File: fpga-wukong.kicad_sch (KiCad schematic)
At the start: 2 parts, among them J4 QMTECH FPGA Module U4, J5 QMTECH FPGA Module U5

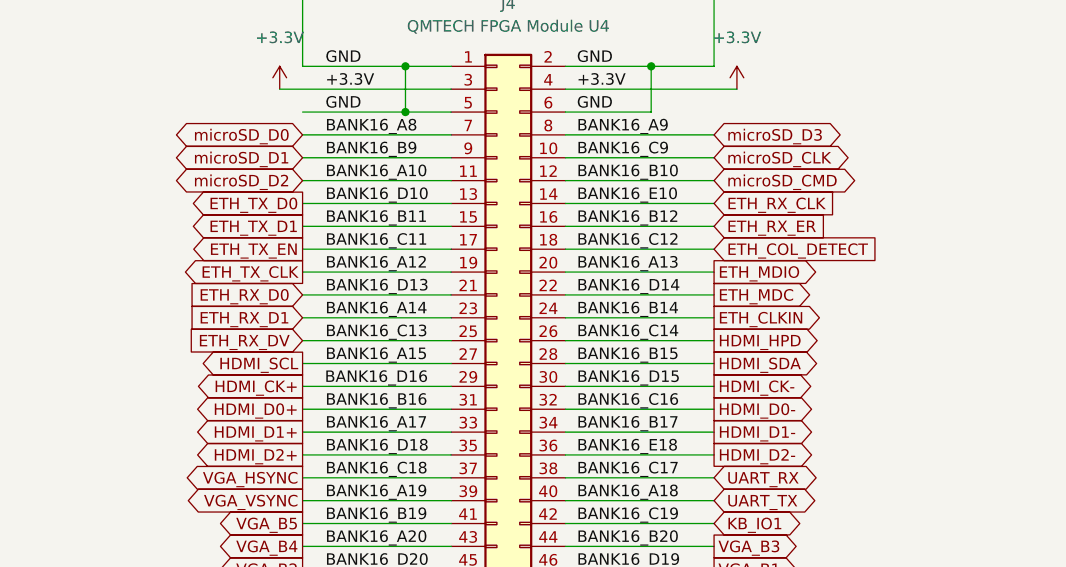
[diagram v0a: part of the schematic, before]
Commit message: layout more of HDMI and ETH and surrounding areas
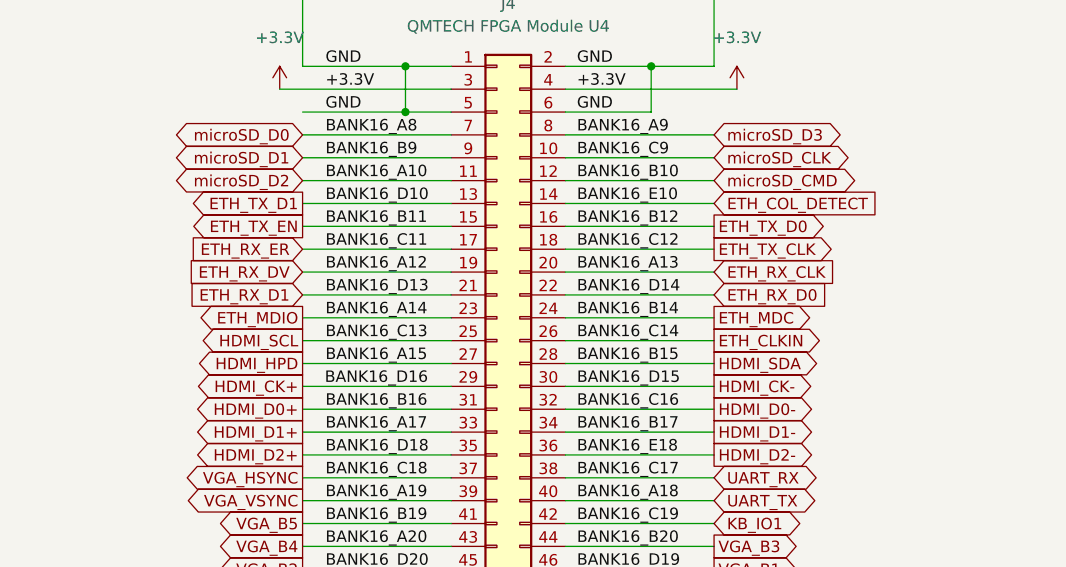
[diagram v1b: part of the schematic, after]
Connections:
- net ETH_CLKIN: now also J4.26 (Pin_26); no longer J4.24 (Pin_24)
- net ETH_COL_DETECT: now also J4.14 (Pin_14); no longer J4.18 (Pin_18)
- net ETH_MDC: now also J4.24 (Pin_24); no longer J4.22 (Pin_22)
- net ETH_MDIO: now also J4.23 (Pin_23); no longer J4.20 (Pin_20)
- net ETH_RX_CLK: now also J4.20 (Pin_20); no longer J4.14 (Pin_14)
- net ETH_RX_D0: now also J4.22 (Pin_22); no longer J4.21 (Pin_21)
- net ETH_RX_D1: now also J4.21 (Pin_21); no longer J4.23 (Pin_23)
- net ETH_RX_DV: now also J4.19 (Pin_19); no longer J4.25 (Pin_25)
- net ETH_RX_ER: now also J4.17 (Pin_17); no longer J4.16 (Pin_16)
- net ETH_TX_CLK: now also J4.18 (Pin_18); no longer J4.19 (Pin_19)
- net ETH_TX_D0: now also J4.16 (Pin_16); no longer J4.13 (Pin_13)
- net ETH_TX_D1: now also J4.13 (Pin_13); no longer J4.15 (Pin_15)
- net ETH_TX_EN: now also J4.15 (Pin_15); no longer J4.17 (Pin_17)
- net HDMI_HPD: now also J4.27 (Pin_27); no longer J4.26 (Pin_26)
- net HDMI_SCL: now also J4.25 (Pin_25); no longer J4.27 (Pin_27)
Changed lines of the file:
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@@
     )
   )
-  (global_label "ETH_MDC" (shape output) (at 106.045 73.025 0) (fields_autoplaced)
-    (effects (font (size 1.27 1.27)) (justify left))
-    (property "Intersheet References" "${INTERSHEET_REFS}" (id 0) (at 116.8643 72.9456 0)
+  (global_label "ETH_MDC" (shape output) (at 106.045 75.565 0) (fields_autoplaced)
+    (effects (font (size 1.27 1.27)) (justify left))
+    (property "Intersheet References" "${INTERSHEET_REFS}" (id 0) (at 116.8643 75.6444 0)
       (effects (font (size 1.27 1.27)) (justify left) hide)
     )
@@
     )
   )
-  (global_label "HDMI_HPD" (shape output) (at 106.045 78.105 0) (fields_autoplaced)
-    (effects (font (size 1.27 1.27)) (justify left))
-    (property "Intersheet References" "${INTERSHEET_REFS}" (id 0) (at 117.9529 78.0256 0)
-      (effects (font (size 1.27 1.27)) (justify left) hide)
+  (global_label "HDMI_HPD" (shape output) (at 60.325 80.645 180) (fields_autoplaced)
+    (effects (font (size 1.27 1.27)) (justify right))
+    (property "Intersheet References" "${INTERSHEET_REFS}" (id 0) (at 48.4171 80.5656 0)
+      (effects (font (size 1.27 1.27)) (justify right) hide)
     )
   )
@@
     )
   )
-  (global_label "ETH_RX_D0" (shape input) (at 60.325 73.025 180) (fields_autoplaced)
-    (effects (font (size 1.27 1.27)) (justify right))
-    (property "Intersheet References" "${INTERSHEET_REFS}" (id 0) (at 47.5705 72.9456 0)
-      (effects (font (size 1.27 1.27)) (justify right) hide)
+  (global_label "ETH_RX_D0" (shape input) (at 106.045 73.025 0) (fields_autoplaced)
+    (effects (font (size 1.27 1.27)) (justify left))
+    (property "Intersheet References" "${INTERSHEET_REFS}" (id 0) (at 118.7995 73.1044 0)
+      (effects (font (size 1.27 1.27)) (justify left) hide)
     )
   )
@@
     )
   )
-  (global_label "ETH_TX_EN" (shape output) (at 60.325 67.945 180) (fields_autoplaced)
-    (effects (font (size 1.27 1.27)) (justify right))
-    (property "Intersheet References" "${INTERSHEET_REFS}" (id 0) (at 47.8729 67.8656 0)
+  (global_label "ETH_TX_EN" (shape output) (at 60.325 65.405 180) (fields_autoplaced)
+    (effects (font (size 1.27 1.27)) (justify right))
+    (property "Intersheet References" "${INTERSHEET_REFS}" (id 0) (at 47.8729 65.3256 0)
       (effects (font (size 1.27 1.27)) (justify right) hide)
     )
@@
     )
   )
-  (global_label "ETH_MDIO" (shape output) (at 106.045 70.485 0) (fields_autoplaced)
-    (effects (font (size 1.27 1.27)) (justify left))
-    (property "Intersheet References" "${INTERSHEET_REFS}" (id 0) (at 117.5295 70.4056 0)
-      (effects (font (size 1.27 1.27)) (justify left) hide)
-    )
-  )
-  (global_label "ETH_RX_D1" (shape input) (at 60.325 75.565 180) (fields_autoplaced)
-    (effects (font (size 1.27 1.27)) (justify right))
-    (property "Intersheet References" "${INTERSHEET_REFS}" (id 0) (at 47.5705 75.4856 0)
-      (effects (font (size 1.27 1.27)) (justify right) hide)
-    )
-  )
-  (global_label "ETH_TX_D1" (shape output) (at 60.325 65.405 180) (fields_autoplaced)
-    (effects (font (size 1.27 1.27)) (justify right))
-    (property "Intersheet References" "${INTERSHEET_REFS}" (id 0) (at 47.8729 65.3256 0)
-      (effects (font (size 1.27 1.27)) (justify right) hide)
-    )
-  )
-  (global_label "HDMI_SCL" (shape output) (at 60.325 80.645 180) (fields_autoplaced)
-    (effects (font (size 1.27 1.27)) (justify right))
-    (property "Intersheet References" "${INTERSHEET_REFS}" (id 0) (at 48.78 80.5656 0)
+  (global_label "ETH_MDIO" (shape output) (at 60.325 75.565 180) (fields_autoplaced)
+    (effects (font (size 1.27 1.27)) (justify right))
+    (property "Intersheet References" "${INTERSHEET_REFS}" (id 0) (at 48.8405 75.6444 0)
+      (effects (font (size 1.27 1.27)) (justify right) hide)
+    )
+  )
+  (global_label "ETH_RX_D1" (shape input) (at 60.325 73.025 180) (fields_autoplaced)
+    (effects (font (size 1.27 1.27)) (justify right))
+    (property "Intersheet References" "${INTERSHEET_REFS}" (id 0) (at 47.5705 73.1044 0)
+      (effects (font (size 1.27 1.27)) (justify right) hide)
+    )
+  )
+  (global_label "ETH_TX_D1" (shape output) (at 60.325 62.865 180) (fields_autoplaced)
+    (effects (font (size 1.27 1.27)) (justify right))
+    (property "Intersheet References" "${INTERSHEET_REFS}" (id 0) (at 47.8729 62.7856 0)
+      (effects (font (size 1.27 1.27)) (justify right) hide)
+    )
+  )
+  (global_label "HDMI_SCL" (shape output) (at 60.325 78.105 180) (fields_autoplaced)
+    (effects (font (size 1.27 1.27)) (justify right))
+    (property "Intersheet References" "${INTERSHEET_REFS}" (id 0) (at 48.78 78.0256 0)
       (effects (font (size 1.27 1.27)) (justify right) hide)
     )
@@
     )
   )
-  (global_label "ETH_TX_D0" (shape output) (at 60.325 62.865 180) (fields_autoplaced)
-    (effects (font (size 1.27 1.27)) (justify right))
-    (property "Intersheet References" "${INTERSHEET_REFS}" (id 0) (at 47.8729 62.7856 0)
-      (effects (font (size 1.27 1.27)) (justify right) hide)
+  (global_label "ETH_TX_D0" (shape output) (at 106.045 65.405 0) (fields_autoplaced)
+    (effects (font (size 1.27 1.27)) (justify left))
+    (property "Intersheet References" "${INTERSHEET_REFS}" (id 0) (at 118.4971 65.3256 0)
+      (effects (font (size 1.27 1.27)) (justify left) hide)
     )
   )
@@
     )
   )
-  (global_label "ETH_CLKIN" (shape output) (at 106.045 75.565 0) (fields_autoplaced)
-    (effects (font (size 1.27 1.27)) (justify left))
-    (property "Intersheet References" "${INTERSHEET_REFS}" (id 0) (at 118.3762 75.4856 0)
-      (effects (font (size 1.27 1.27)) (justify left) hide)
-    )
-  )
-  (global_label "ETH_TX_CLK" (shape output) (at 60.325 70.485 180) (fields_autoplaced)
-    (effects (font (size 1.27 1.27)) (justify right))
-    (property "Intersheet References" "${INTERSHEET_REFS}" (id 0) (at 46.7843 70.4056 0)
-      (effects (font (size 1.27 1.27)) (justify right) hide)
+  (global_label "ETH_CLKIN" (shape output) (at 106.045 78.105 0) (fields_autoplaced)
+    (effects (font (size 1.27 1.27)) (justify left))
+    (property "Intersheet References" "${INTERSHEET_REFS}" (id 0) (at 118.3762 78.0256 0)
+      (effects (font (size 1.27 1.27)) (justify left) hide)
+    )
+  )
+  (global_label "ETH_TX_CLK" (shape output) (at 106.045 67.945 0) (fields_autoplaced)
+    (effects (font (size 1.27 1.27)) (justify left))
+    (property "Intersheet References" "${INTERSHEET_REFS}" (id 0) (at 119.5857 67.8656 0)
+      (effects (font (size 1.27 1.27)) (justify left) hide)
     )
   )
@@
     )
   )
-  (global_label "ETH_RX_DV" (shape input) (at 60.325 78.105 180) (fields_autoplaced)
-    (effects (font (size 1.27 1.27)) (justify right))
-    (property "Intersheet References" "${INTERSHEET_REFS}" (id 0) (at 47.6914 78.0256 0)
-      (effects (font (size 1.27 1.27)) (justify right) hide)
-    )
-  )
-  (global_label "ETH_RX_ER" (shape input) (at 106.045 65.405 0) (fields_autoplaced)
-    (effects (font (size 1.27 1.27)) (justify left))
-    (property "Intersheet References" "${INTERSHEET_REFS}" (id 0) (at 118.7391 65.3256 0)
-      (effects (font (size 1.27 1.27)) (justify left) hide)
+  (global_label "ETH_RX_DV" (shape input) (at 60.325 70.485 180) (fields_autoplaced)
+    (effects (font (size 1.27 1.27)) (justify right))
+    (property "Intersheet References" "${INTERSHEET_REFS}" (id 0) (at 47.6914 70.4056 0)
+      (effects (font (size 1.27 1.27)) (justify right) hide)
+    )
+  )
+  (global_label "ETH_RX_ER" (shape input) (at 60.325 67.945 180) (fields_autoplaced)
+    (effects (font (size 1.27 1.27)) (justify right))
+    (property "Intersheet References" "${INTERSHEET_REFS}" (id 0) (at 47.6309 67.8656 0)
+      (effects (font (size 1.27 1.27)) (justify right) hide)
     )
   )
@@
     )
   )
-  (global_label "ETH_RX_CLK" (shape input) (at 106.045 62.865 0) (fields_autoplaced)
-    (effects (font (size 1.27 1.27)) (justify left))
-    (property "Intersheet References" "${INTERSHEET_REFS}" (id 0) (at 119.8881 62.7856 0)
+  (global_label "ETH_RX_CLK" (shape input) (at 106.045 70.485 0) (fields_autoplaced)
+    (effects (font (size 1.27 1.27)) (justify left))
+    (property "Intersheet References" "${INTERSHEET_REFS}" (id 0) (at 119.8881 70.4056 0)
       (effects (font (size 1.27 1.27)) (justify left) hide)
     )
@@
     )
   )
-  (global_label "ETH_COL_DETECT" (shape input) (at 106.045 67.945 0) (fields_autoplaced)
-    (effects (font (size 1.27 1.27)) (justify left))
-    (property "Intersheet References" "${INTERSHEET_REFS}" (id 0) (at 124.2424 67.8656 0)
-      (effects (font (size 1.27 1.27)) (justify left) hide)
-    )
+  (global_label "ETH_COL_DETECT" (shape input) (at 106.045 62.865 0) (fields_autoplaced)
+    (effects (font (size 1.27 1.27)) (justify left))
+    (property "Intersheet References" "${INTERSHEET_REFS}" (id 0) (at 124.2424 62.7856 0)
+      (effects (font (size 1.27 1.27)) (justify left) hide)
+    )

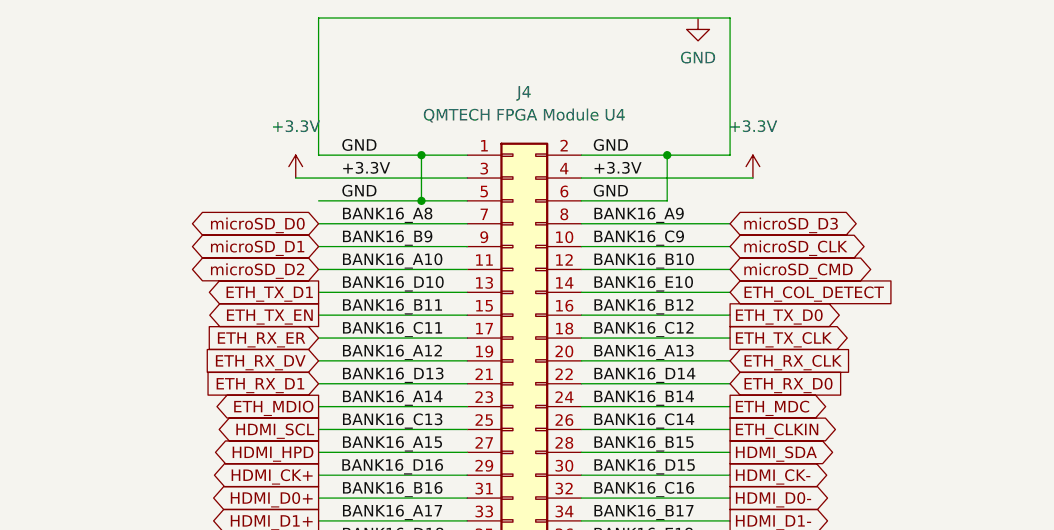
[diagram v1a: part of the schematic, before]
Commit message: route microSD card
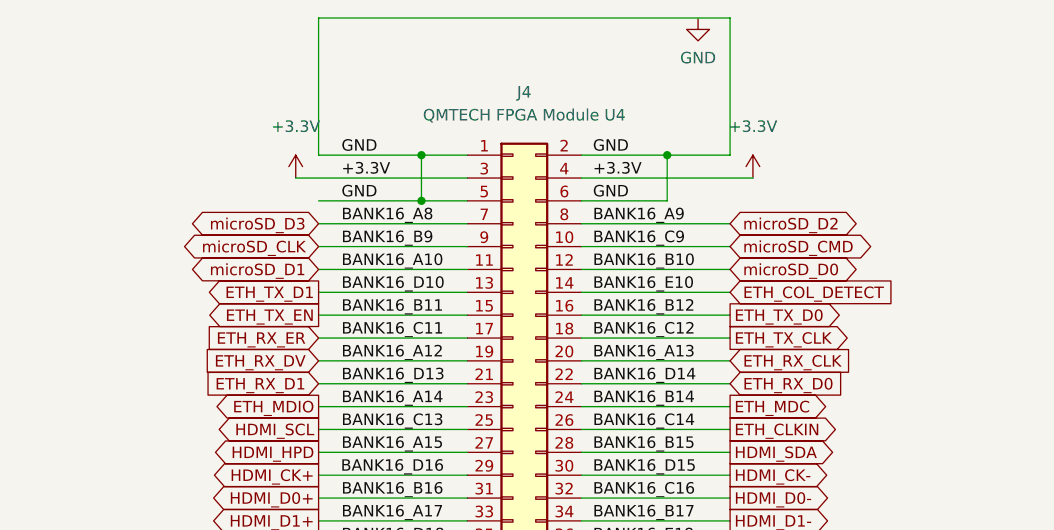
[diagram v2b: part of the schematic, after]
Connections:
- net microSD_CLK: now also J4.9 (Pin_9); no longer J4.10 (Pin_10)
- net microSD_CMD: now also J4.10 (Pin_10); no longer J4.12 (Pin_12)
- net microSD_D0: now also J4.12 (Pin_12); no longer J4.7 (Pin_7)
- net microSD_D1: now also J4.11 (Pin_11); no longer J4.9 (Pin_9)
- net microSD_D2: now also J4.8 (Pin_8); no longer J4.11 (Pin_11)
- net microSD_D3: now also J4.7 (Pin_7); no longer J4.8 (Pin_8)

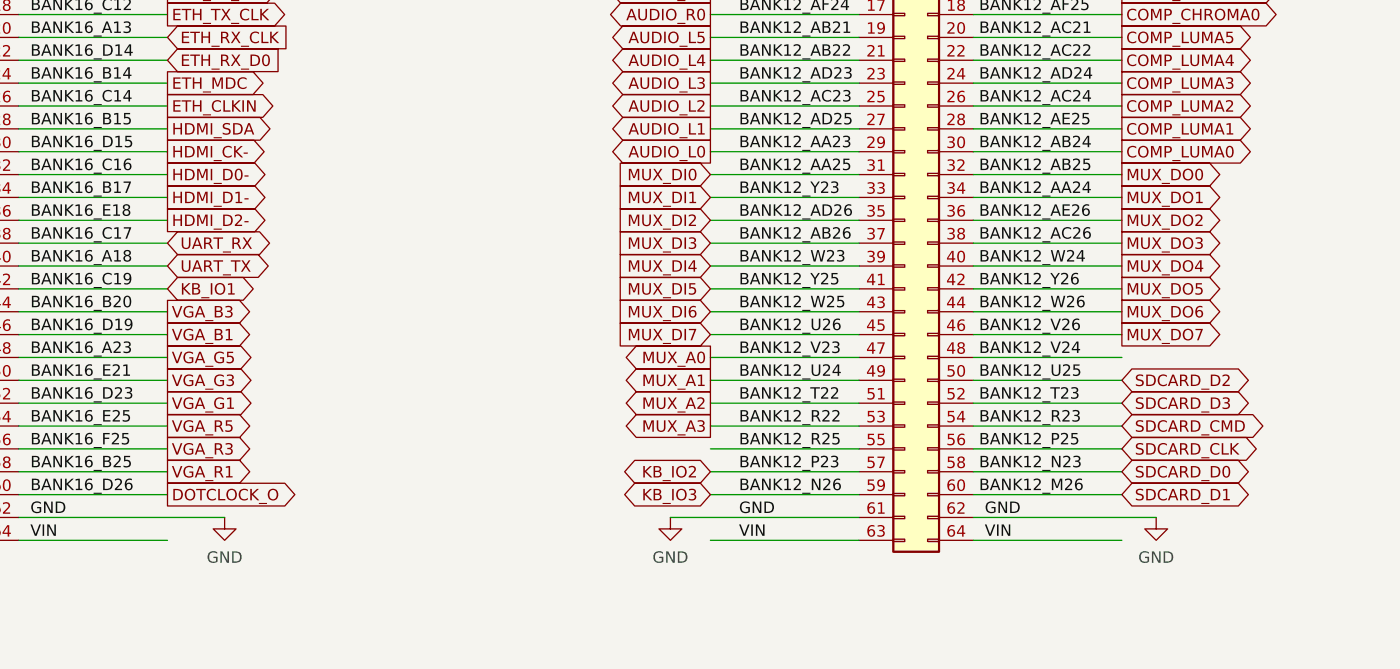
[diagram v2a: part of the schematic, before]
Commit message: route hi MUX address lines
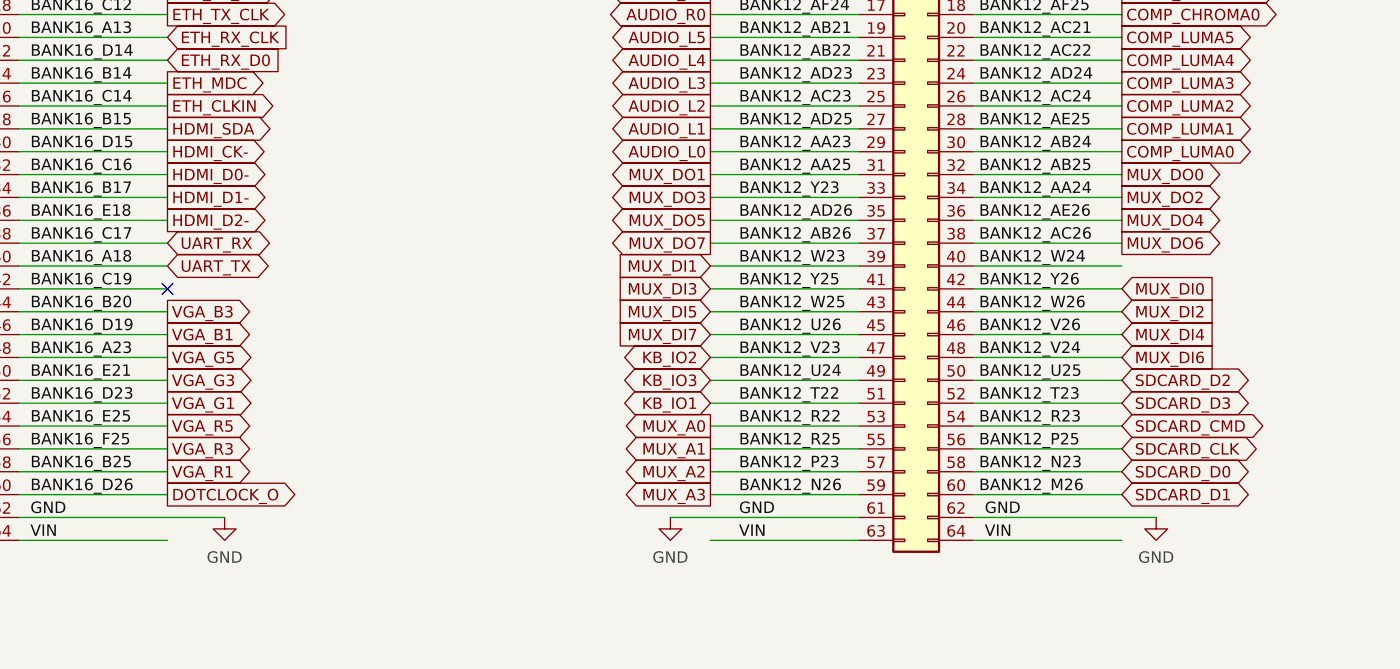
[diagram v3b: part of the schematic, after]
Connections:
- net BANK12_R25 is gone; now on net MUX_A1: J5.55 (Pin_55)
- net BANK12_V24 is gone; now on net MUX_DI6: J5.48 (Pin_48)
- net KB_IO1: now also J5.51 (Pin_51); no longer J4.42 (Pin_42)
- net KB_IO2: now also J5.47 (Pin_47); no longer J5.57 (Pin_57)
- net KB_IO3: now also J5.49 (Pin_49); no longer J5.59 (Pin_59)
- net MUX_A0: now also J5.53 (Pin_53); no longer J5.47 (Pin_47)
- net MUX_A1: no longer J5.49 (Pin_49)
- net MUX_A2: now also J5.57 (Pin_57); no longer J5.51 (Pin_51)
- net MUX_A3: now also J5.59 (Pin_59); no longer J5.53 (Pin_53)
- net MUX_DI0: now also J5.42 (Pin_42); no longer J5.31 (Pin_31)
- net MUX_DI1: now also J5.39 (Pin_39); no longer J5.33 (Pin_33)
- net MUX_DI2: now also J5.44 (Pin_44); no longer J5.35 (Pin_35)
- net MUX_DI3: now also J5.41 (Pin_41); no longer J5.37 (Pin_37)
- net MUX_DI4: now also J5.46 (Pin_46); no longer J5.39 (Pin_39)
- net MUX_DI5: now also J5.43 (Pin_43); no longer J5.41 (Pin_41)
- net MUX_DI6: no longer J5.43 (Pin_43)
- net MUX_DO1: now also J5.31 (Pin_31); no longer J5.34 (Pin_34)
- net MUX_DO2: now also J5.34 (Pin_34); no longer J5.36 (Pin_36)
- net MUX_DO3: now also J5.33 (Pin_33); no longer J5.38 (Pin_38)
- net MUX_DO4: now also J5.36 (Pin_36); no longer J5.40 (Pin_40)
- net MUX_DO5: now also J5.35 (Pin_35); no longer J5.42 (Pin_42)
- net MUX_DO6: now also J5.38 (Pin_38); no longer J5.44 (Pin_44)
- net MUX_DO7: now also J5.37 (Pin_37); no longer J5.46 (Pin_46)
- new net BANK12_W24: J5.40 (Pin_40)
- new net BANK16_C19: J4.42 (Pin_42)
- no-connect marks 0 -> 1
